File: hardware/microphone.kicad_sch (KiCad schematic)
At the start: 3 parts

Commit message: r and c footprint change
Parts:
- C1: footprint Capacitor_SMD:C_0201_0603Metric -> Capacitor_SMD:C_0603_1608Metric
- R1: value 1k -> 1K; footprint Resistor_SMD:R_0201_0603Metric -> Resistor_SMD:R_0603_1608Metric
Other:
- moved on the sheet: MIC.CASE1

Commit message: minor schematic changes
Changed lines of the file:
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@@
 	(wire
 		(pts
-			(xy 163.83 87.63) (xy 182.88 87.63)
+			(xy 163.83 87.63) (xy 186.69 87.63)
 		)
 		(stroke
@@
 		)
 	)
-	(hierarchical_label "GPIO11"
+	(global_label "GPIO11"
 		(shape input)
-		(at 182.88 87.63 0)
+		(at 186.69 87.63 0)
+		(fields_autoplaced yes)
 		(effects
 			(font
 				(size 1.27 1.27)
-				(thickness 0.254)
-				(bold yes)
 			)
 			(justify left)
 		)
+		(property "Intersheetrefs" "${INTERSHEET_REFS}"
+			(at 196.5695 87.63 0)
+			(effects
+				(font
+					(size 1.27 1.27)
+				)
+				(justify left)
+				(hide yes)
+			)
+		)
 	)

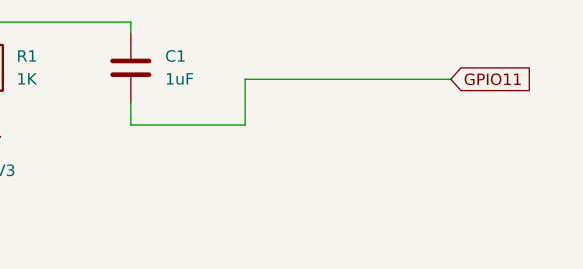
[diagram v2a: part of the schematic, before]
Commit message: type of connections changed
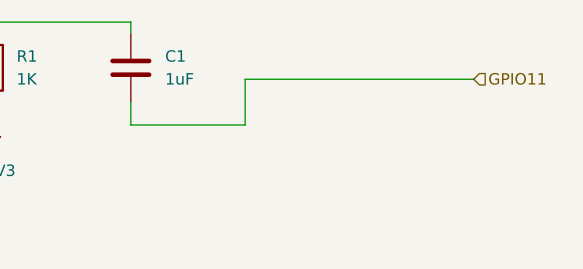
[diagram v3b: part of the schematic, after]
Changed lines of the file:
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@@
 	(wire
 		(pts
-			(xy 163.83 87.63) (xy 186.69 87.63)
+			(xy 163.83 87.63) (xy 189.23 87.63)
 		)
 		(stroke
@@
 		)
 	)
-	(global_label "GPIO11"
+	(hierarchical_label "GPIO11"
 		(shape input)
-		(at 186.69 87.63 0)
-		(fields_autoplaced yes)
+		(at 189.23 87.63 0)
 		(effects
 			(font
@@
 			(justify left)
 		)
-		(property "Intersheetrefs" "${INTERSHEET_REFS}"
-			(at 196.5695 87.63 0)
-			(effects
-				(font
-					(size 1.27 1.27)
-				)
-				(justify left)
-				(hide yes)
-			)
-		)
 	)
